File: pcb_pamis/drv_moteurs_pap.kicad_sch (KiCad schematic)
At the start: 16 parts, among them J3 Conn_01x04, J4 Conn_01x04, J5 Conn_01x04, U3 TMC2209_SILENTSTEPSTICK, U4 TMC2209_SILENTSTEPSTICK, U5 TMC2209_SILENTSTEPSTICK

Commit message: Ajout empreinte condo couché + réparation contour PCB avec 7mm autour des trous de fixation
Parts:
- C10, C8, C9: footprint Capacitor_THT:CP_Radial_D5.0mm_P2.00mm -> w_capacitors:CP_6.3x11mm_horiz-L
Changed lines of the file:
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@@
 			)
 		)
-		(property "Footprint" "Capacitor_THT:CP_Radial_D5.0mm_P2.00mm"
+		(property "Footprint" "w_capacitors:CP_6.3x11mm_horiz-L"
 			(at 146.05 138.43 0)
 			(effects
@@
 			)
 		)
-		(property "Footprint" "Capacitor_THT:CP_Radial_D5.0mm_P2.00mm"
+		(property "Footprint" "w_capacitors:CP_6.3x11mm_horiz-L"
 			(at 146.05 44.45 0)
 			(effects
@@
 			)
 		)
-		(property "Footprint" "Capacitor_THT:CP_Radial_D5.0mm_P2.00mm"
+		(property "Footprint" "w_capacitors:CP_6.3x11mm_horiz-L"
 			(at 146.05 91.44 0)
 			(effects

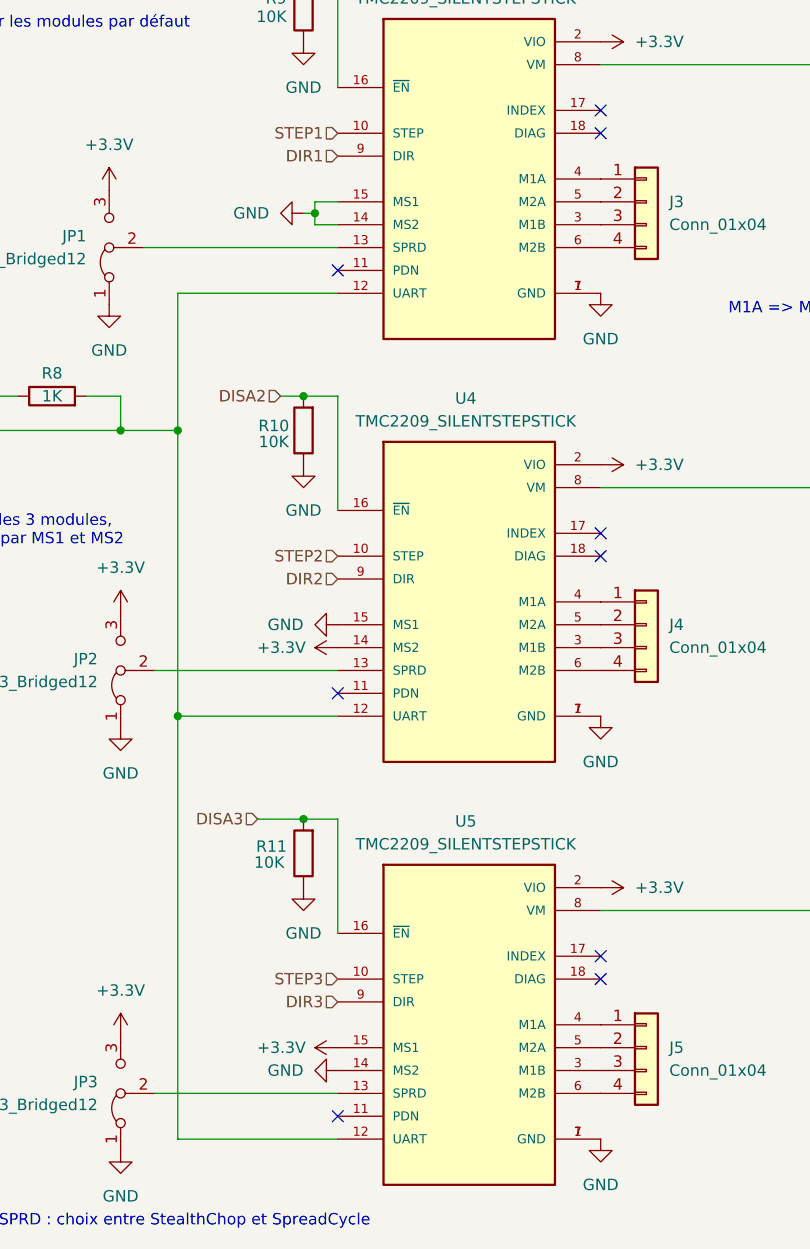
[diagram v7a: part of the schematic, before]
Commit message: Ajout BAU servo PAMI, finitions PCB Actionneurs, fichier fab stencil. Version commandée PAMI & Actionneurs
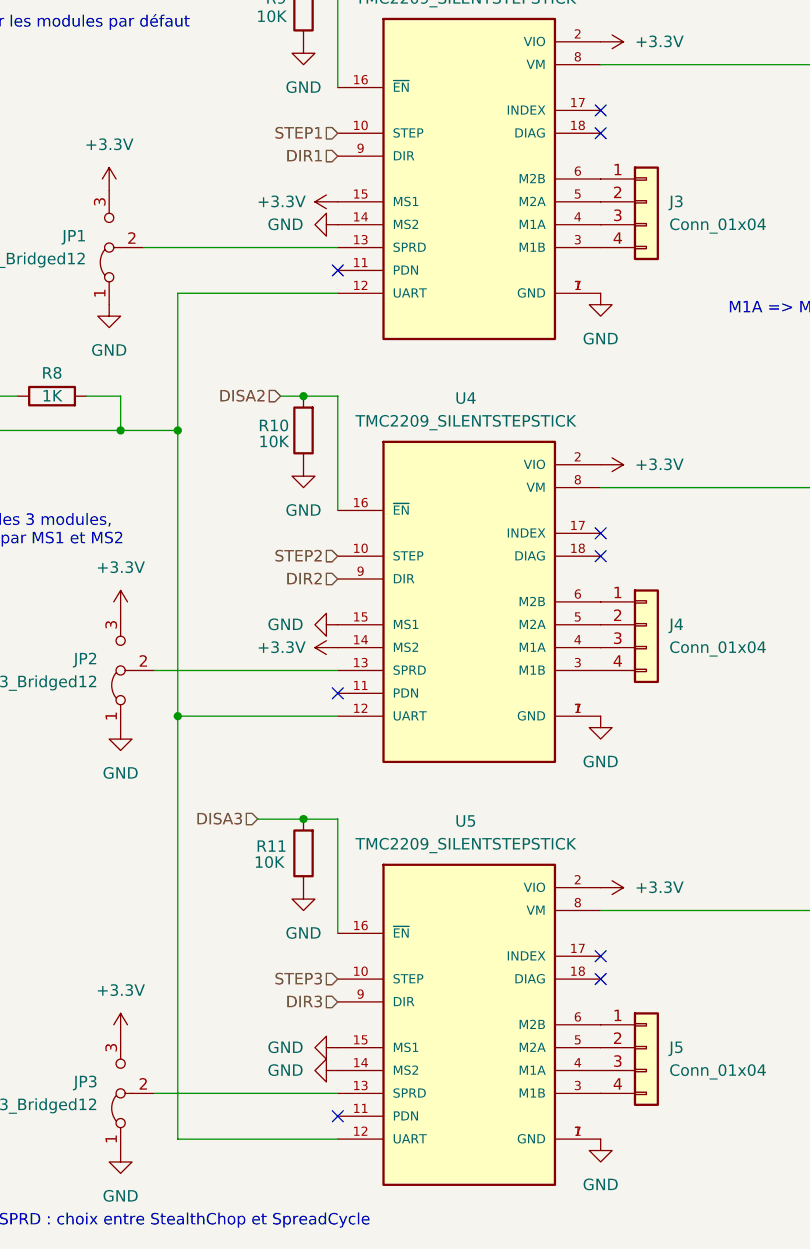
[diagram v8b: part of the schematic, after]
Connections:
- net +3.3V: now also U3.15 (MS1); no longer U5.15 (MS1)
- net GND: now also U5.15 (MS1); no longer U3.15 (MS1)
- net at U5.3 (M1B): now also J5.4 (Pin_4); no longer J5.3 (Pin_3)
- net at U5.4 (M1A): now also J5.3 (Pin_3); no longer J5.1 (Pin_1)
- net at U5.6 (M2B): now also J5.1 (Pin_1); no longer J5.4 (Pin_4)
- net at U4.3 (M1B): now also J4.4 (Pin_4); no longer J4.3 (Pin_3)
- net at U4.4 (M1A): now also J4.3 (Pin_3); no longer J4.1 (Pin_1)
- net at U4.6 (M2B): now also J4.1 (Pin_1); no longer J4.4 (Pin_4)
- net at U3.3 (M1B): now also J3.4 (Pin_4); no longer J3.3 (Pin_3)
- net at U3.4 (M1A): now also J3.3 (Pin_3); no longer J3.1 (Pin_1)
- net at U3.6 (M2B): now also J3.1 (Pin_1); no longer J3.4 (Pin_4)
